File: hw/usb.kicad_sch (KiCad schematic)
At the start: 3 parts

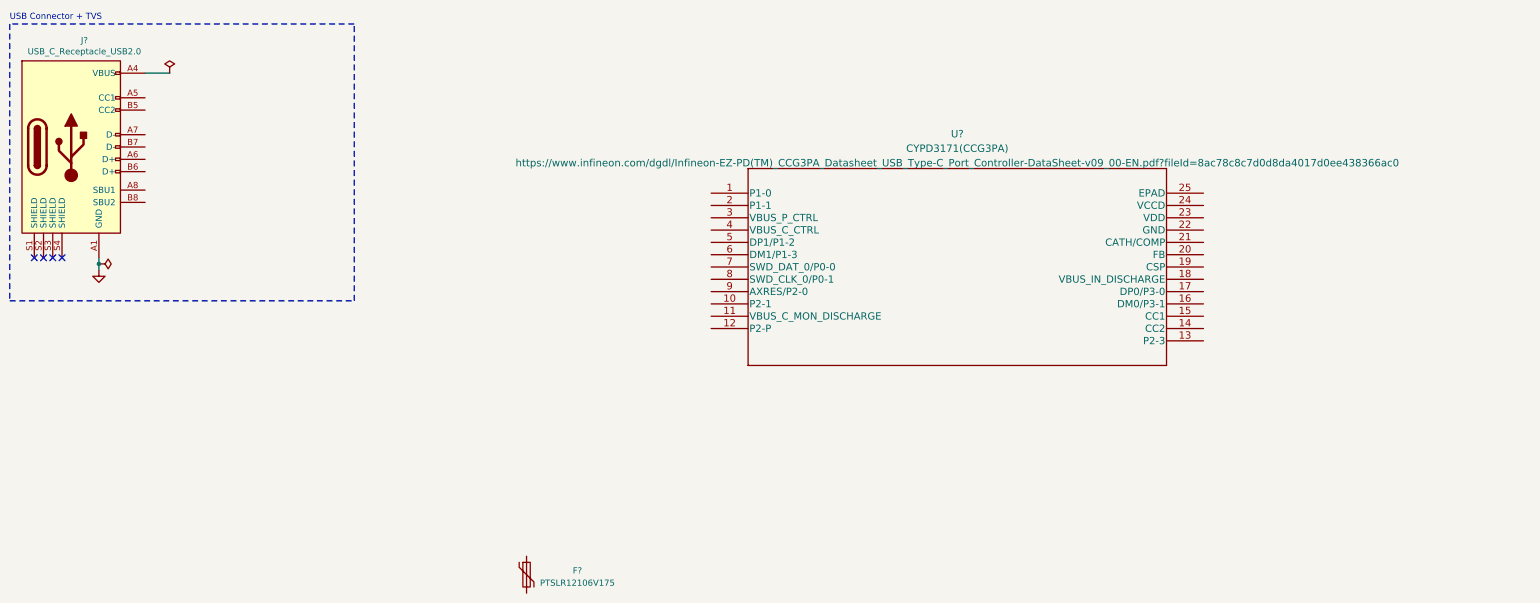
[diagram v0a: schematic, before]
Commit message: Cypress USB interface symbol & Layout needs fixing
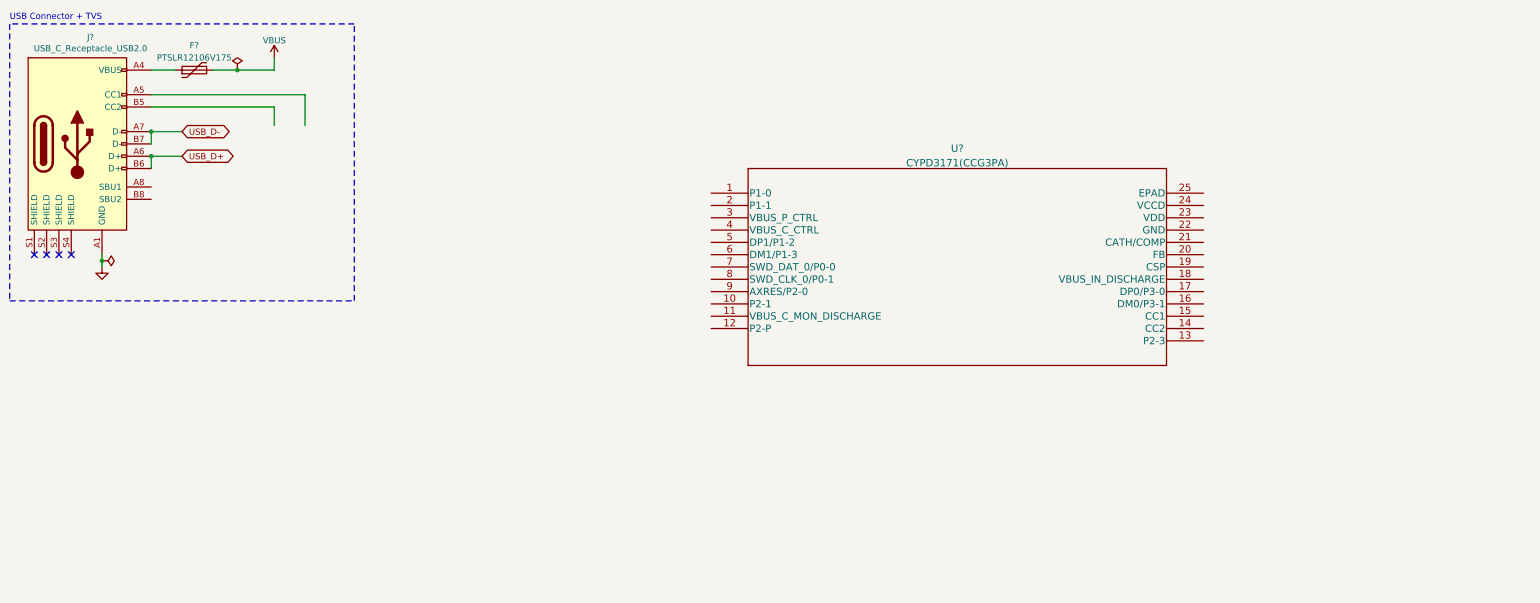
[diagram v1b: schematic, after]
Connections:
- net at F?.1: now also J?.A4 (VBUS)
- net VBUS: now reaches F?.2
- net USB_D+: now reaches J?.A6 (D+)
- net USB_D+: now also J?.B6 (D+)
- net USB_D-: now reaches J?.A7 (D-)
- net USB_D-: now also J?.B7 (D-)
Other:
- moved on the sheet: F?, J?
